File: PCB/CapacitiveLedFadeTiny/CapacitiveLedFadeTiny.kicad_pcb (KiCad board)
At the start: 2 copper layers, 36.3 x 36.3 mm, 7 parts, among them J4 Antenna, U1 ATTINY85-20SU

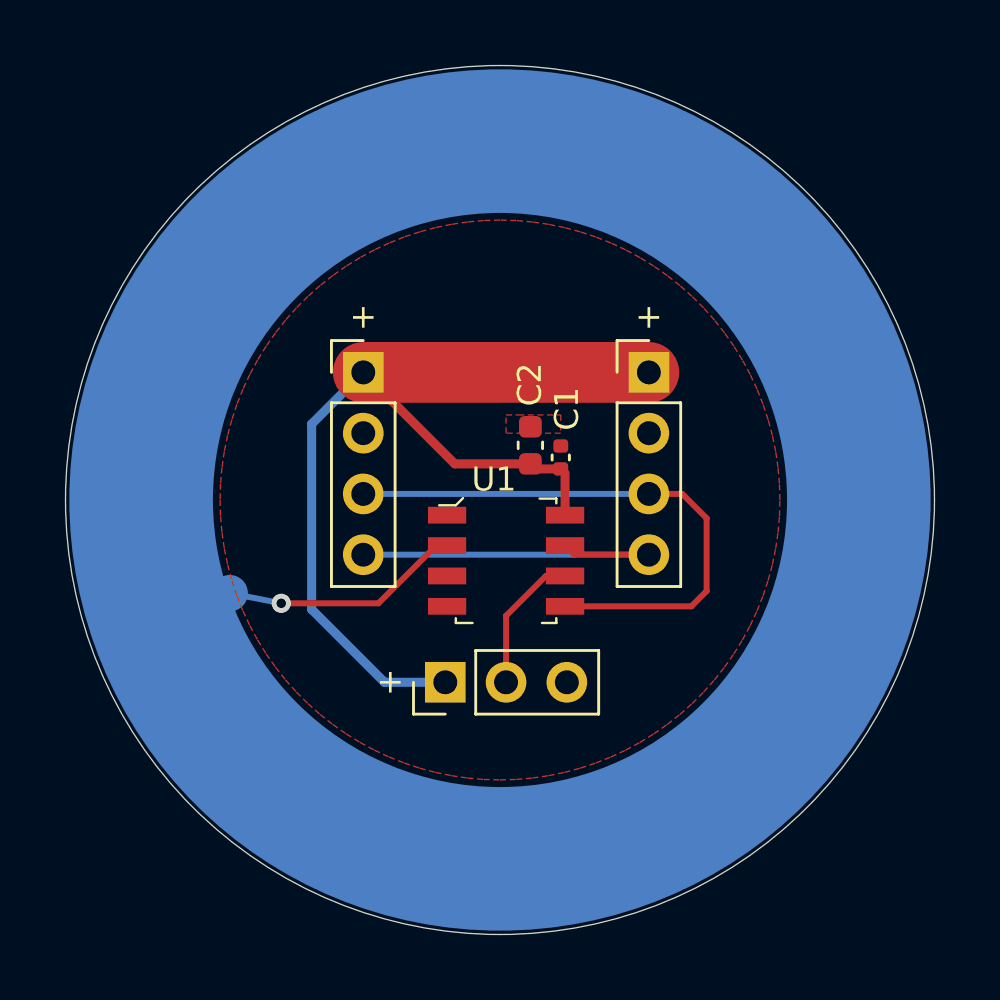
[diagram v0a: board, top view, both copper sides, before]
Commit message: Update board layout
the attiny is actually a wider footprint :kms:
this is why we do prototype boards
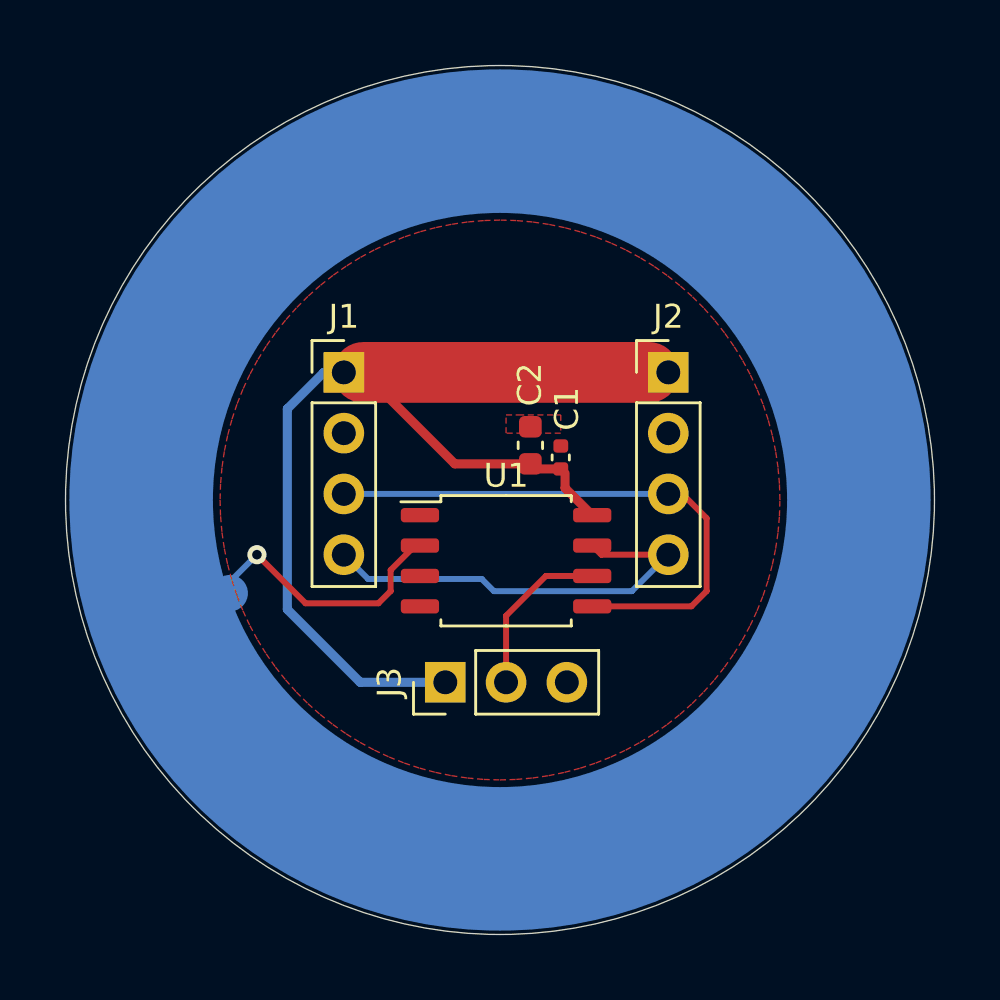
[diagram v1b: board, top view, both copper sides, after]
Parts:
- U1: footprint digikey-footprints:SOIC-8_W5.3mm -> Package_SO:SOIC-8_5.23x5.23mm_P1.27mm
- moved J2 0.81 mm to (136.1, 91.2)
- moved J1 0.81 mm to (122.5, 91.2)
- renumbered + to J1, + to J2, + to J3
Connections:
- J4 pad 1: (no net) -> Net-(J4-Pin_1)
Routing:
- net VCC: track 41.5 -> 43.6 mm
- net /SCLK: track 15.6 -> 17.4 mm
- net Net-(J3-Pin_2): track 5.93 -> 7.07 mm
- net Net-(J4-Pin_1): track 10.1 -> 11.1 mm

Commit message: v2 of I2C board
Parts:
- added 1: 1, Library:TestPoint_Pad_1.5mm_circular, F.Cu at (115.3, 97.3)
- added 2: 2, Library:TestPoint_Pad_1.5mm_circular, F.Cu at (113.0, 98.6)
- added 3: 3, Library:TestPoint_Pad_1.5mm_circular, F.Cu at (118.6, 108.7)
- added 6: 6, Library:TestPoint_Pad_1.5mm_circular, F.Cu at (130.0, 110.5)
- added GND: GND, Library:TestPoint_Pad_1.5mm_circular, F.Cu at (137.9, 102.4)
- added SCLK: SCLK, Library:TestPoint_Pad_1.5mm_circular, F.Cu at (138.2, 108.2)
- added SDA: SDA, Library:TestPoint_Pad_1.5mm_circular, F.Cu at (139.2, 85.1)
- added Screw: Power Inject, Library:SCREW_TERMINAL_5mm_01x02, F.Cu at (138.2, 93.8)
- added VCC: VCC, Library:TestPoint_Pad_1.5mm_circular, F.Cu at (123.4, 81.8)
- ATTiny85: renamed from U1; footprint Package_SO:SOIC-8_5.23x5.23mm_P1.27mm -> ATTINY85-20SFR:SOIC127P798X216-8N
- BusIn1: renamed from J1; footprint Connector_PinHeader_2.54mm:PinHeader_1x04_P2.54mm_Vertical -> Connector_JST:JST_XH_B4B-XH-A_1x04_P2.50mm_Vertical
- BusOut1: renamed from J2; footprint Connector_PinHeader_2.54mm:PinHeader_1x04_P2.54mm_Vertical -> Connector_JST:JST_XH_B4B-XH-A_1x04_P2.50mm_Vertical
- J3: footprint Connector_PinHeader_2.54mm:PinHeader_1x03_P2.54mm_Vertical -> Connector_JST:JST_XH_B3B-XH-A_1x03_P2.50mm_Vertical
- moved C1 13.3 mm to (118.9, 98.6)
- moved ATTiny85 11.2 mm to (118.6, 102.6)
- moved C2 10.0 mm to (121.4, 98.9), turned to 180 degrees
- moved BusOut1 6.14 mm to (131.1, 87.6), turned to -90 degrees
- moved BusIn1 3.84 mm to (124.0, 87.6), turned to -90 degrees
- moved J3 1.17 mm to (127.3, 103.1), turned to 0 degrees
- turned J4 to 0 degrees
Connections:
- net Net-(J3-Pin_2) renamed /6
- net Net-(J4-Pin_1) renamed /2
- ATTiny85 pad 1: unconnected-(U1-PB5-Pad1) -> /1
- ATTiny85 pad 3: unconnected-(U1-PB4-Pad3) -> /3
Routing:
- net /SDA: track 23.7 -> 44.4 mm, vias 0 -> 3
- net /SCLK: track 17.4 -> 32.8 mm, vias 0 -> 3
- net VCC: track 43.6 -> 54.6 mm
- net /6: track 7.07 -> 15.8 mm, vias 0 -> 1
- net /3: track 0.00 -> 7.47 mm
- net /1: track 0.00 -> 3.56 mm
- net /2: track 11.1 -> 12.8 mm
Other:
- board text added: "+"
- board text added: "-"

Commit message: Add programmer board for v2
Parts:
- moved 2 5.98 mm to (114.1, 92.7)
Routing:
- net /2: track 12.8 -> 19.3 mm
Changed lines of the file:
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@@
   (net 8 "/3")
   (footprint "Library:TestPoint_Pad_1.5mm_circular" (layer "F.Cu")
-    (at 113.03 98.552)
+    (at 114.0714 92.6592)
     (descr "SMD rectangular pad as test Point, square 1.5mm side length")
     (tags "test point SMD pad rectangle square")
@@
   (gr_circle (center 139.192 85.09) (end 139.4968 84.1756)
     (stroke (width 0.15) (type default)) (fill none) (layer "User.1"))
-  (gr_circle (center 113.03 98.552) (end 112.522 97.7392)
+  (gr_circle (center 114.0714 92.6592) (end 115.029892 92.6592)
     (stroke (width 0.15) (type default)) (fill none) (layer "User.1"))
   (gr_text "+" (at 142.24 97.028) (layer "F.SilkS")
@@
   (segment (start 126.746 105.664) (end 127.237 105.664) (width 0.381) (layer "B.Cu") (net 5))
   (segment (start 127.237 105.664) (end 129.794 103.107) (width 0.381) (layer "B.Cu") (net 5))
+  (segment (start 112.5982 100.9142) (end 112.776 101.092) (width 0.25) (layer "F.Cu") (net 6))
   (segment (start 113.665 101.981) (end 112.776 101.092) (width 0.381) (layer "F.Cu") (net 6))
-  (segment (start 112.776 98.806) (end 113.03 98.552) (width 0.381) (layer "F.Cu") (net 6))
-  (segment (start 112.776 101.092) (end 112.776 98.806) (width 0.381) (layer "F.Cu") (net 6))
+  (segment (start 114.0714 92.6592) (end 112.5982 94.1324) (width 0.25) (layer "F.Cu") (net 6))
   (segment (start 114.988 101.981) (end 113.665 101.981) (width 0.381) (layer "F.Cu") (net 6))
+  (segment (start 112.5982 94.1324) (end 112.5982 100.9142) (width 0.25) (layer "F.Cu") (net 6))
   (via (at 112.776 101.092) (size 0.8) (drill 0.4) (layers "F.Cu" "B.Cu") (net 6))
   (segment (start 112.776 101.092) (end 112.776 97.776) (width 0.381) (layer "B.Cu") (net 6))
@@
         (xy 147.1132 98.220623)
         (xy 147.173039 97.371247)
-        (xy 147.193 96.52)
       )
     )
-  )
-  (zone (net 2) (net_name "GND") (layer "F.Cu") (hatch edge 0.5)
-    (priority 1)
-    (connect_pads yes (clearance 0.5))
-    (min_thickness 0.25) (filled_areas_thickness no)
-    (fill yes (thermal_gap 0.5) (thermal_bridge_width 0.5))
-    (polygon
-      (pts
-        (xy 129.286 92.964)
-        (xy 129.794 92.964)
-        (xy 131.572 92.964)
-        (xy 131.572 93.726)
-        (xy 129.286 93.726)
-      )
-    )

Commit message: v3 pcb
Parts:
- removed 1: 1, Library:TestPoint_Pad_1.5mm_circular
- removed 2: 2, Library:TestPoint_Pad_1.5mm_circular
- removed 3: 3, Library:TestPoint_Pad_1.5mm_circular
- removed 6: 6, Library:TestPoint_Pad_1.5mm_circular
- removed ATTiny85: ATTINY85-20SU, ATTINY85-20SFR:SOIC127P798X216-8N
- removed BusIn1: Bus In, Connector_JST:JST_XH_B4B-XH-A_1x04_P2.50mm_Vertical
- removed C1: 1uF, Capacitor_SMD:C_0402_1005Metric
- removed C2: 0.1uF, Capacitor_SMD:C_0603_1608Metric
- removed J3: LEDs, Connector_JST:JST_XH_B3B-XH-A_1x03_P2.50mm_Vertical
- removed J4: Antenna, TestPoint:TestPoint_Pad_1.0x1.0mm
- removed Screw: Power Inject, Library:SCREW_TERMINAL_5mm_01x02
- added BUS: Bus In, Connector_JST:JST_SH_BM04B-SRSS-TB_1x04-1MP_P1.00mm_Vertical, F.Cu at (126.3, 88.9)
- added C3: 0.1uf, Capacitor_SMD:C_0402_1005Metric, F.Cu at (123.5, 94.6)
- added C4: 1uf, Capacitor_SMD:C_0603_1608Metric, F.Cu at (124.8, 94.9)
- added J1: Antenna, CapacitiveLedFadeLibrary:CapacitiveAntenna, F.Cu at (177.1, 85.3)
- added J6: Power Inject, Library:2Pad, F.Cu at (131.9, 105.3)
- added LED: LEDs, Connector_JST:JST_SH_BM03B-SRSS-TB_1x03-1MP_P1.00mm_Vertical, F.Cu at (118.3, 98.8)
- added O_LED: ~, CapacitiveLedFadeLibrary:SK6805-EC15, F.Cu at (118.3, 103.3)
- added RX: PadRX, Library:TestPoint_Pad_1.5mm_circular, F.Cu at (125.9, 106.9)
- added STA: ~, CapacitiveLedFadeLibrary:SK6805-EC15, F.Cu at (130.8, 101.2)
- added TX: PadTX, Library:TestPoint_Pad_1.5mm_circular, F.Cu at (123.5, 99.6)
- added U1: ATtiny3224-X, Package_SO:TSSOP-14_4.4x5mm_P0.65mm, F.Cu at (129.7, 96.2)
- added UPDI: PadUPDI, Library:TestPoint_Pad_1.5mm_circular, F.Cu at (137.9, 92.8)
- BusOut1: footprint Connector_JST:JST_XH_B4B-XH-A_1x04_P2.50mm_Vertical -> Connector_JST:JST_SH_BM04B-SRSS-TB_1x04-1MP_P1.00mm_Vertical
- moved GND 16.3 mm to (121.7, 104.1)
- moved VCC 9.23 mm to (120.8, 90.6)
- moved SCLK 5.90 mm to (137.9, 102.3)
- moved SDA 4.80 mm to (137.3, 89.5)
- moved BusOut1 1.38 mm to (131.6, 88.9), turned to 90 degrees
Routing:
- net GND: track 0.00 -> 63.8 mm, vias 0 -> 4
- net Net-(LED1-VDD): track 0.00 -> 24.0 mm
- net /2: track 19.3 -> 0.00 mm, vias 1 -> 0
- net /SDA: track 44.4 -> 25.5 mm, vias 3 -> 0
- net /LED_Signal: track 0.00 -> 17.6 mm, vias 0 -> 2
- net /6: track 15.8 -> 0.00 mm, vias 1 -> 0
- net Net-(J1-Pin_1): track 0.00 -> 13.6 mm, vias 0 -> 1
- net /RX: track 0.00 -> 9.83 mm
- net Net-(LED2-DIN): track 0.00 -> 9.29 mm
- net VCC: track 54.6 -> 47.0 mm, vias 0 -> 2
- net /3: track 7.47 -> 0.00 mm
- net /UPDI: track 0.00 -> 7.04 mm
- net /SCLK: track 32.8 -> 28.5 mm
- net /TX: track 0.00 -> 4.15 mm
- net /1: track 3.56 -> 0.00 mm
- removed copper zone on F.Cu, net GND
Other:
- board text added: "CapacitiveLedFadeTiny v3 JBrooksbank 2025"
- board text removed: "+"
- board text removed: "-"

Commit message: pcb v3.1
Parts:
- GND, RX, SCLK, SDA, TX, UPDI, VCC: moved to B.Cu
- moved J6 16.6 mm to (119.5, 94.1), turned to -90 degrees
- moved SDA 12.7 mm to (124.6, 90.3), turned to 180 degrees
- moved LED 12.1 mm to (129.4, 103.5)
- moved SCLK 11.5 mm to (133.8, 91.5), turned to 180 degrees
- moved GND 11.3 mm to (132.2, 99.8), turned to 180 degrees
- moved LED2 9.34 mm to (129.1, 92.0), turned to 180 degrees
- moved VCC 8.04 mm to (128.8, 90.2), turned to 180 degrees
- moved RX 6.37 mm to (127.0, 100.6), turned to 180 degrees
- moved LED1 6.18 mm to (124.3, 104.7), turned to 180 degrees
- moved UPDI 4.50 mm to (135.7, 96.7), turned to 180 degrees
- moved BusOut1 3.03 mm to (134.6, 89.1)
- moved BusIn1 2.27 mm to (124.0, 89.1)
- moved TX 1.33 mm to (123.8, 98.3), turned to 180 degrees
- moved C3 0.21 mm to (123.6, 94.7)
- moved C4 0.21 mm to (124.9, 95.1)
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- renumbered BUS to BusIn1, O_LED to LED1, STA to LED2
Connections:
- BusIn1 pad 3: /SDA -> /SCLK
- BusIn1 pad 4: /SCLK -> /SDA
- BusOut1 pad 3: /SDA -> /SCLK
- BusOut1 pad 4: /SCLK -> /SDA
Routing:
- net Net-(LED1-VDD): track 24.0 -> 13.1 mm, vias 0 -> 2
- net /SDA: track 25.5 -> 33.2 mm, vias 0 -> 1
- net VCC: track 47.0 -> 41.3 mm, vias 2 -> 1
- net /RX: track 9.83 -> 4.82 mm, vias 0 -> 1
- net /UPDI: track 7.04 -> 3.41 mm, vias 0 -> 1
- net GND: track 63.8 -> 67.0 mm, vias 4 -> 3
- net Net-(LED2-DIN): track 9.29 -> 7.18 mm, vias 0 -> 2
- net /LED_Signal: track 17.6 -> 18.4 mm, vias 2 -> 0
- net /TX: track 4.15 -> 3.52 mm, vias 0 -> 1
- net /SCLK: track 28.5 -> 28.1 mm, vias 3 -> 1
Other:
- outline, holes or cut-outs redrawn
- board text added: "+ -"
- board text added: "SDA SCLK GND VCC"

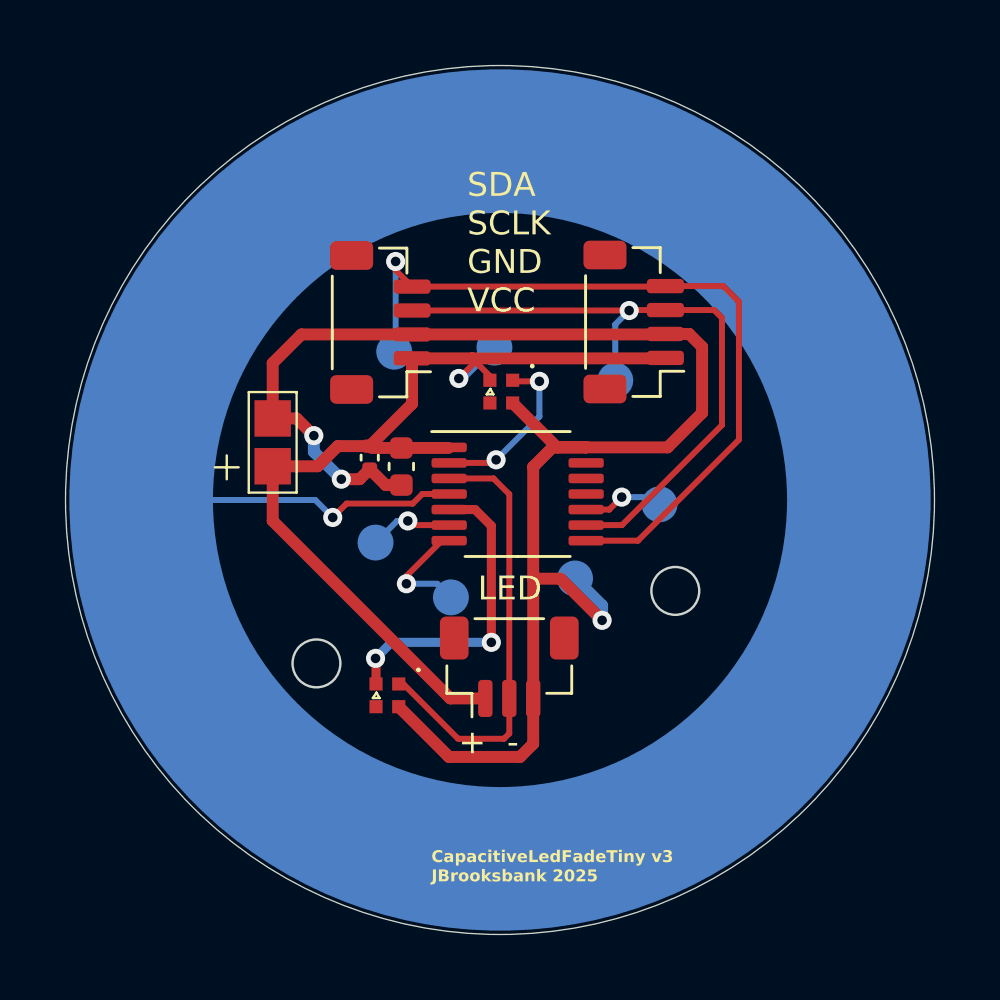
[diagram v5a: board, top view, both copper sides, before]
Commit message: v3.2 pcb, changed to PA connectors
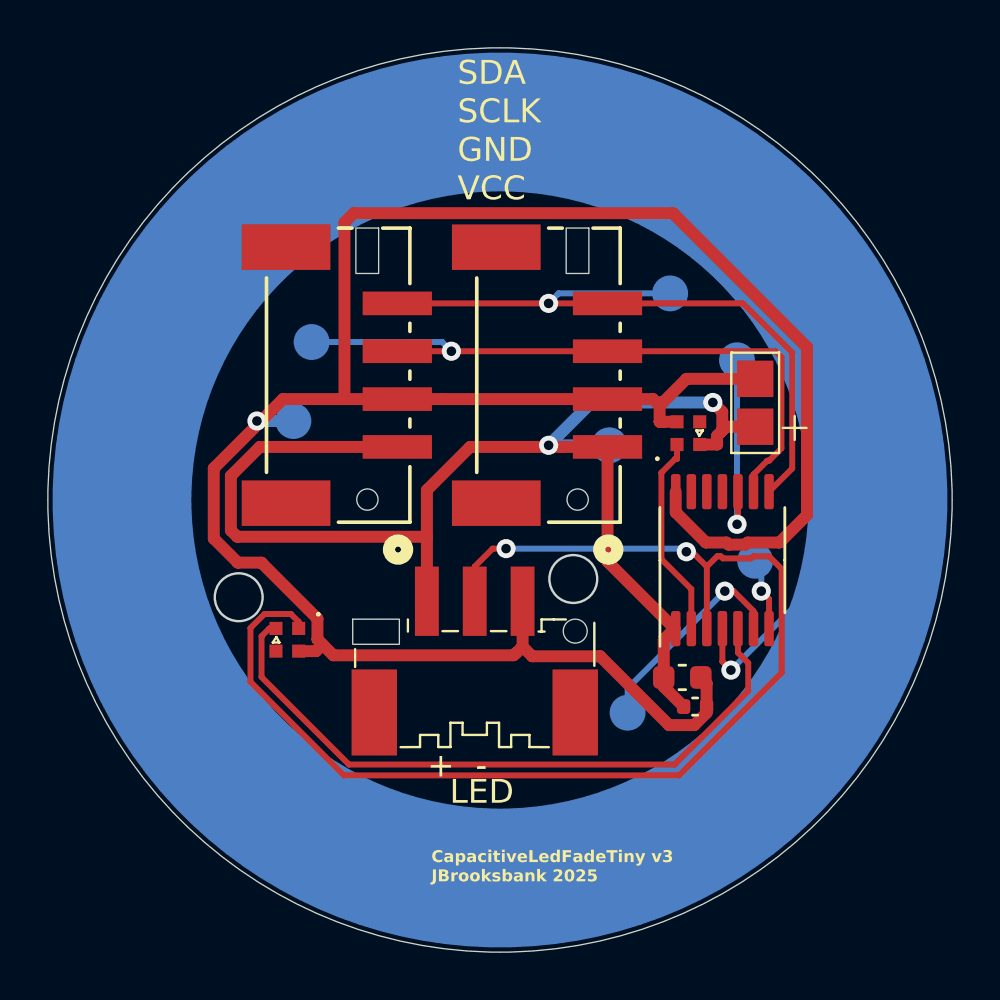
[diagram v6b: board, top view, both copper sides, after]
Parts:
- BusIn1, BusOut1: footprint Connector_JST:JST_SH_BM04B-SRSS-TB_1x04-1MP_P1.00mm_Vertical -> digikey-footprints:CONN_BM04B-PASS-1-TFTLFSN_JST
- LED: footprint Connector_JST:JST_SH_BM03B-SRSS-TB_1x03-1MP_P1.00mm_Vertical -> digikey-footprints:BM03B-PASS-1-TFT
- moved J6 20.2 mm to (139.7, 92.5)
- moved C3 17.1 mm to (137.2, 105.2), turned to 0 degrees
- moved C4 14.7 mm to (136.7, 103.9), turned to 0 degrees
- moved GND 13.5 mm to (120.4, 93.2)
- moved RX 12.8 mm to (139.7, 99.1)
- moved SCLK 12.8 mm to (121.2, 89.9)
- moved TX 12.7 mm to (134.4, 105.4)
- moved SDA 11.8 mm to (136.1, 87.9)
- moved U1 8.99 mm to (138.3, 99.0), turned to 90 degrees
- moved LED2 8.01 mm to (136.9, 93.7), turned to 0 degrees
- moved UPDI 6.84 mm to (138.9, 90.7)
- moved VCC 6.31 mm to (133.6, 94.2)
- moved LED1 4.78 mm to (120.1, 102.4)
- moved BusIn1 3.87 mm to (127.2, 91.3), turned to -90 degrees
- moved LED 3.10 mm to (128.0, 100.8)
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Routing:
- net GND: track 67.0 -> 103.4 mm, vias 3 -> 1
- net /LED_Signal: track 18.4 -> 52.8 mm, vias 0 -> 2
- net VCC: track 41.3 -> 57.9 mm, vias 1 -> 2
- net Net-(LED1-VDD): track 13.1 -> 28.4 mm, vias 2 -> 0
- net /TX: track 3.52 -> 9.04 mm
- net /UPDI: track 3.41 -> 8.24 mm
- net /SDA: track 33.2 -> 28.8 mm
- net Net-(J1-Pin_1): track 13.6 -> 11.2 mm
- net /RX: track 4.82 -> 3.08 mm
- net Net-(LED2-DIN): track 7.18 -> 8.53 mm, vias 2 -> 0
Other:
- board size 36.3 x 36.3 mm -> 37.8 x 37.8 mm
